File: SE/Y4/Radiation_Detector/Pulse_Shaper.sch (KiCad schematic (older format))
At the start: 23 parts, among them U2 OP179GRT, U3 OP179GRT, U4 OP179GRT, U5 OP179GRT

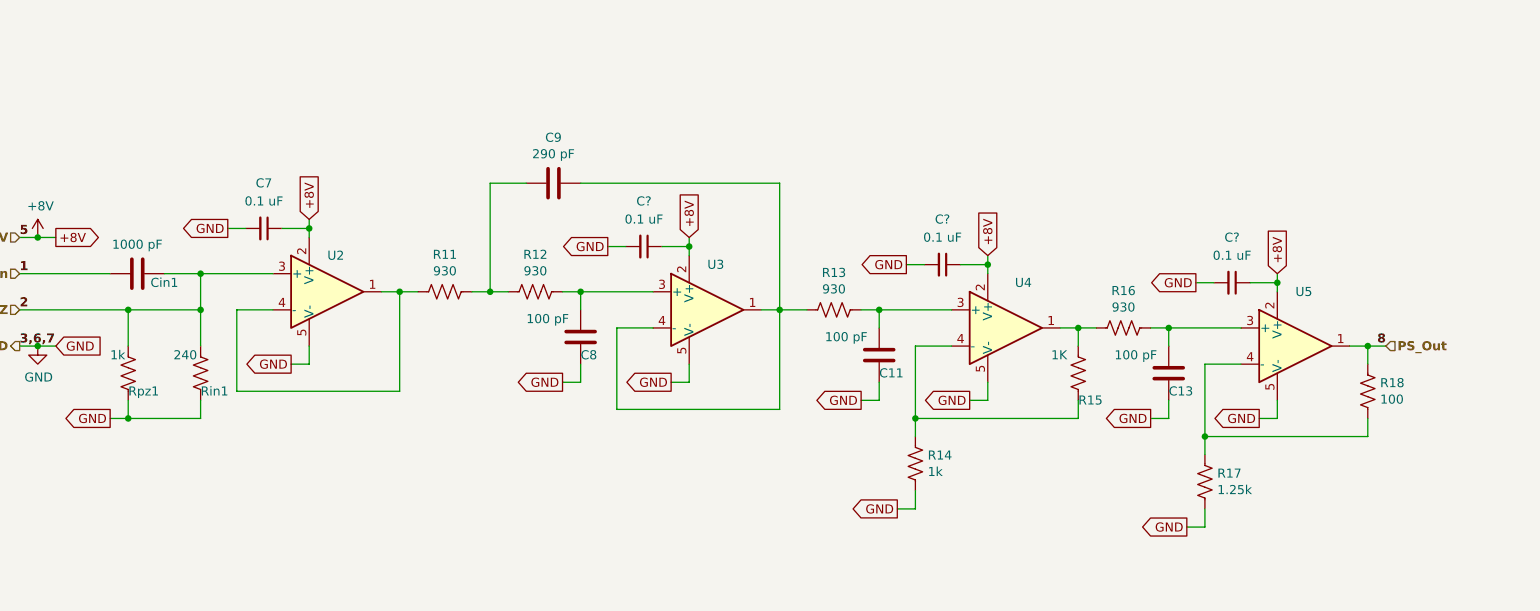
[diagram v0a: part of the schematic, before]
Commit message: SiPM schematic symbol modified
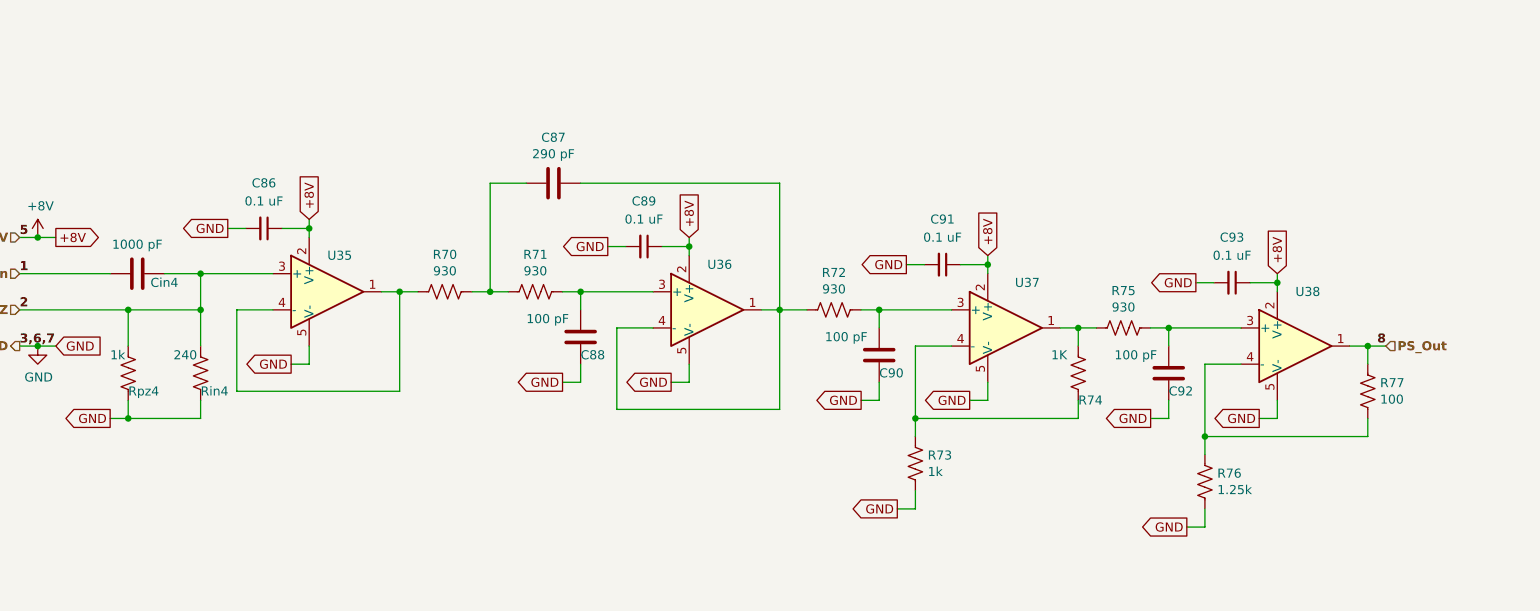
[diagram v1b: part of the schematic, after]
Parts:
- gave numbers to parts that had none: 3

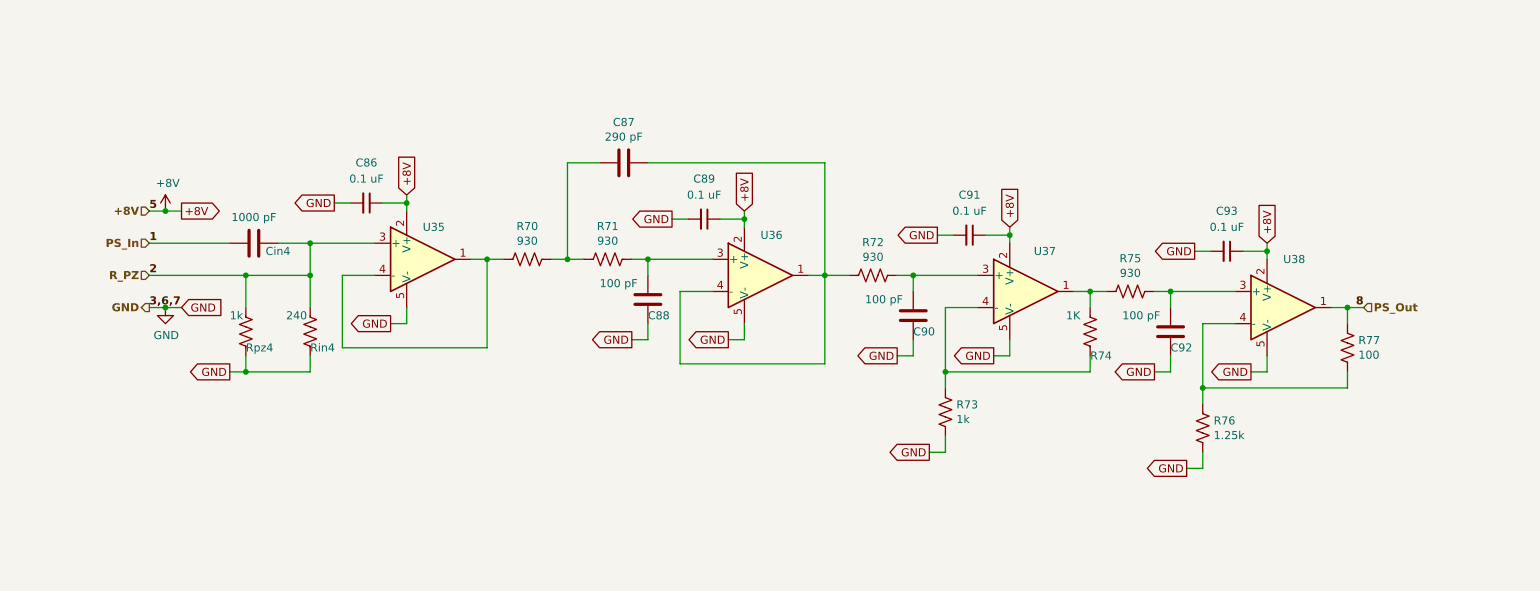
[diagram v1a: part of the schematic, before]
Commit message: cleaned up schematic and clarified
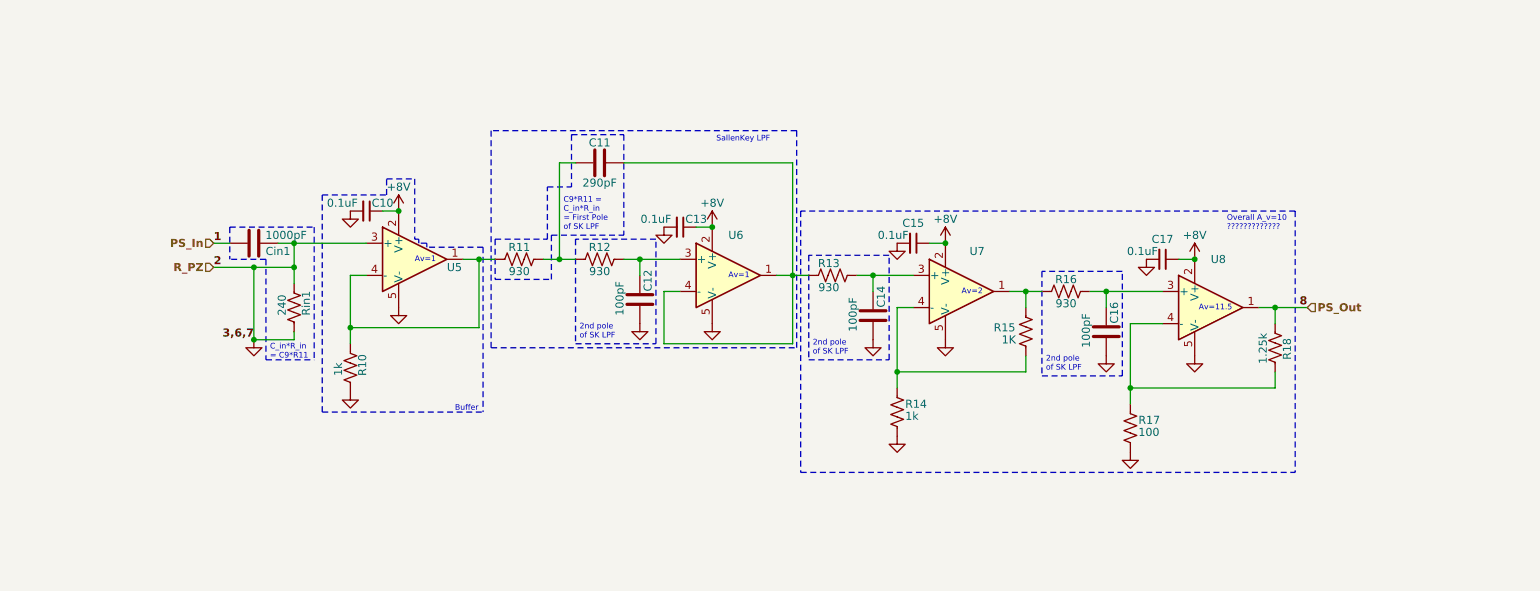
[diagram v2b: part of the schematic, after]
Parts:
- removed Rpz1: 1k, symbol Device:R_US
- added R10: 1k, symbol Device:R_US
- C10: renamed from C7; value 0.1 uF -> 0.1uF
- C11: renamed from C9; value 290 pF -> 290pF
- C12: renamed from C8; value 100 pF -> 100pF
- C13: renamed from C15; value 0.1 uF -> 0.1uF
- C14: renamed from C11; value 100 pF -> 100pF
- C15: renamed from C16; value 0.1 uF -> 0.1uF
- C16: renamed from C13; value 100 pF -> 100pF
- C17: value 0.1 uF -> 0.1uF
- Cin1: value 1000 pF -> 1000pF
- R17: value 1.25k -> 100
- R18: value 100 -> 1.25k
- renumbered U2 to U5, U3 to U6, U4 to U7, U5 to U8
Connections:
- net R_PZ is gone; now on net GND: Cin1.1, Rin1.1, U5.3 (+)
- net GND: now also R10.2
- net at R11.2, U5.1, U5.4 (-): now also R10.1
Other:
- note added: "2nd pole\nof SK LPF"
- note added: "Av=1"
- note added: "Av=11.5"
- note added: "Av=2"
- note added: "Buffer"
- note added: "C9*R11 =\nC_in*R_in\n= First Pole\nof SK LPF"
- note added: "C_in*R_in\n= C9*R11"
- note added: "Overall A_v=10\n?????????????"
- note added: "SallenKey LPF"
- moved on the sheet: C10, C11, C12, C13, C14, C15, C16, R11, R12, R13, R14, R15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

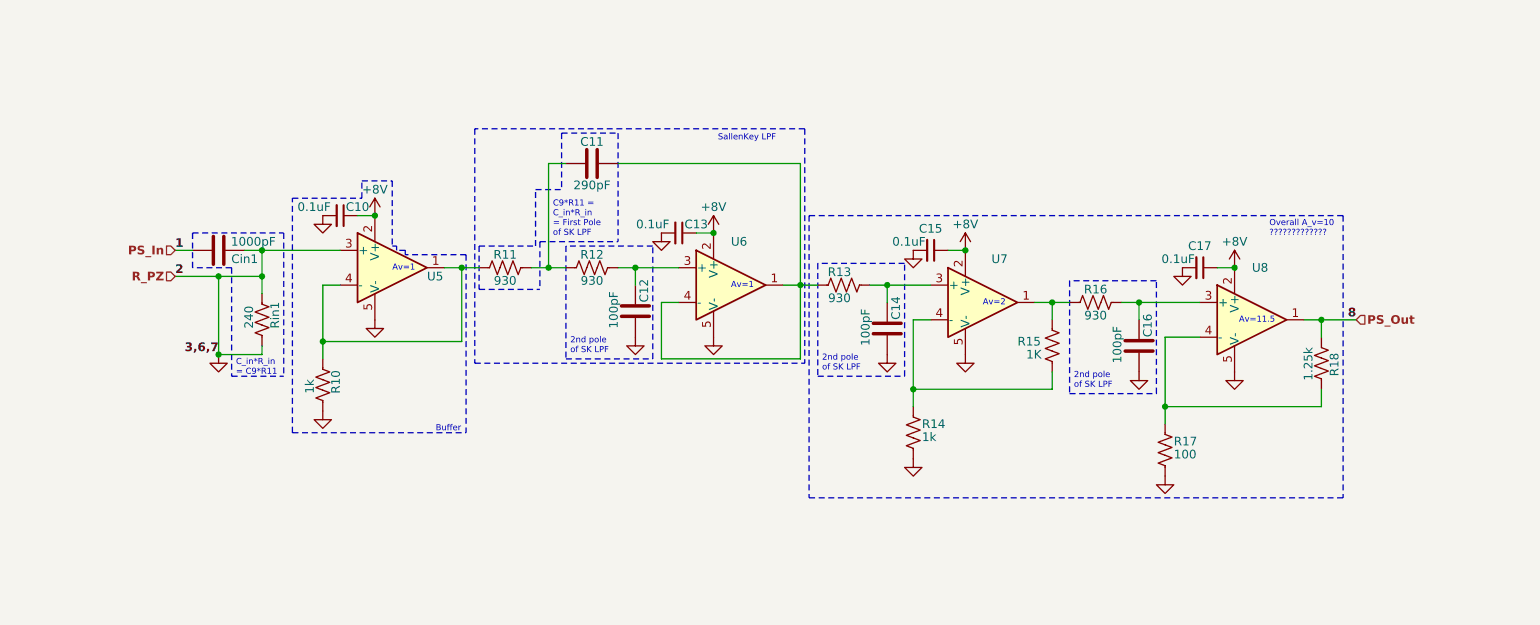
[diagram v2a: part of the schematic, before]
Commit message: updated schematic labeling
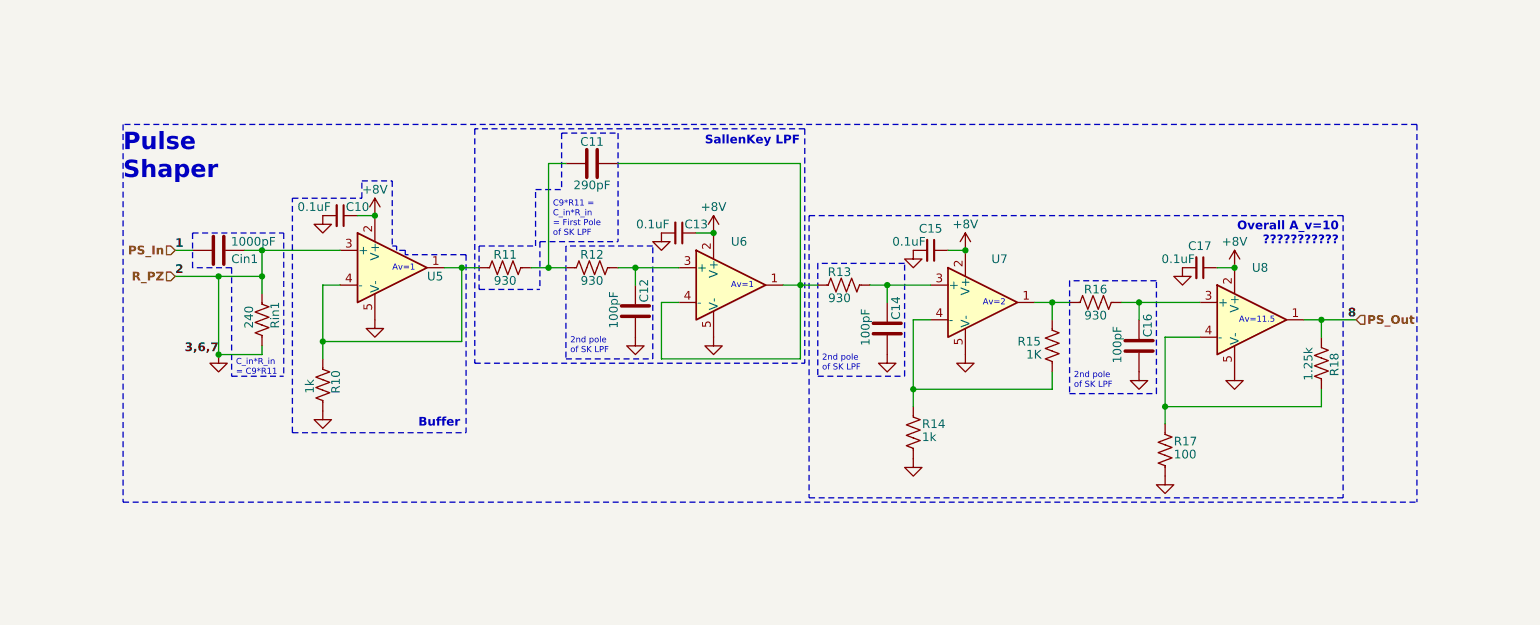
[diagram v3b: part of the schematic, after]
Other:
- note added: "Overall A_v=10\n???????????"
- note added: "Pulse\nShaper"
- note removed: "Overall A_v=10\n?????????????"
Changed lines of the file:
@@
 Wire Notes Line
 	2875 3525 2875 4550
-Text Notes 2700 4550 0    35   ~ 0
+Text Notes 2600 4525 0    50   ~ 10
 Buffer
 Wire Notes Line
@@
 Wire Notes Line
 	4825 2800 4825 4150
-Text Notes 4325 2875 0    35   ~ 0
+Text Notes 4250 2900 0    50   ~ 10
 SallenKey LPF
 Wire Wire Line
@@
 Wire Notes Line
 	7925 3300 7925 4925
-Text Notes 7500 3425 0    35   ~ 0
-Overall A_v=10\n?????????????
+Text Notes 7900 3475 2    50   ~ 10
+Overall A_v=10\n???????????
 Wire Notes Line
 	3950 4125 3950 3475
@@
 Text Notes 4400 3725 0    35   ~ 0
 Av=1
+Text Notes 900  3100 0    100  ~ 20
+Pulse\nShaper
+Wire Notes Line
+	8350 2775 900  2775
+Wire Notes Line
+	900  2775 900  4950
+Wire Notes Line
+	900  4950 8350 4950
+Wire Notes Line
+	8350 2775 8350 4950
 $EndSCHEMATC
